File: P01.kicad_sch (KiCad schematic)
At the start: 63 parts

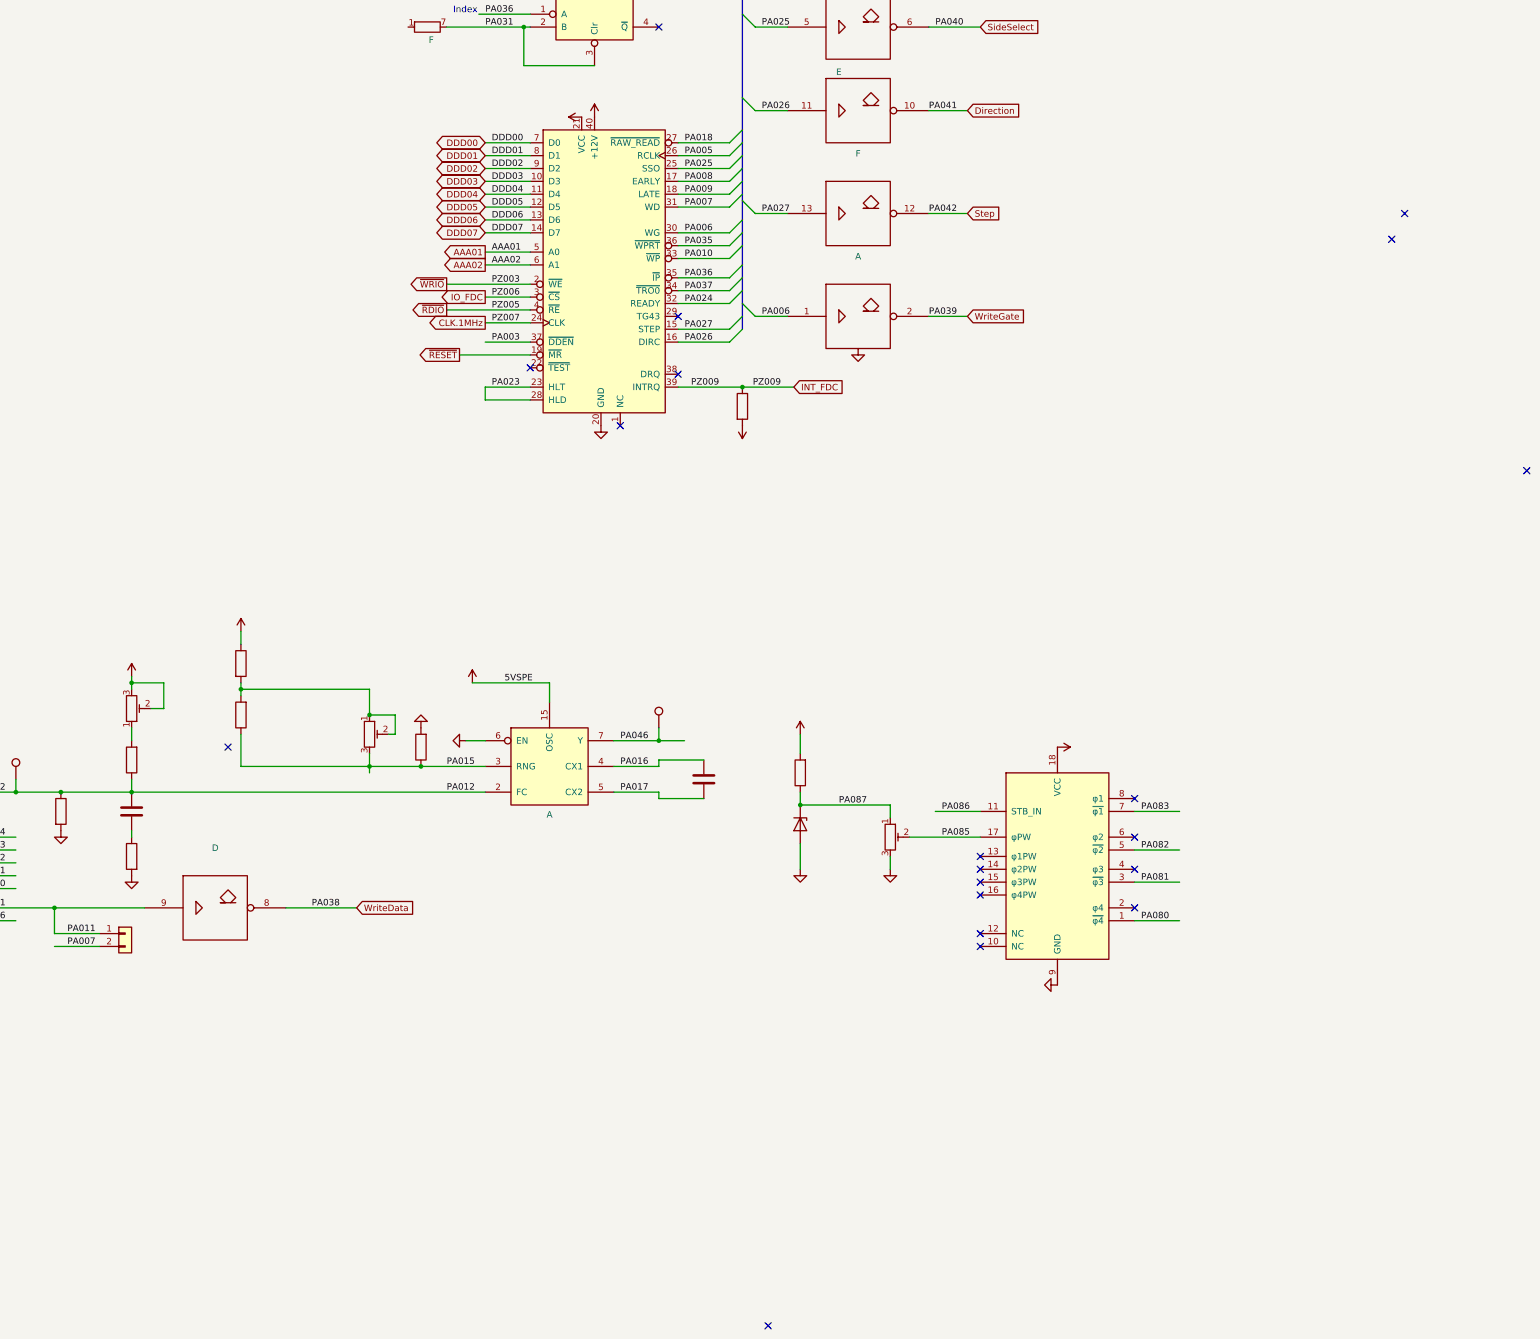
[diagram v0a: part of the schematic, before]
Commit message: fixing KiCad6 warnings
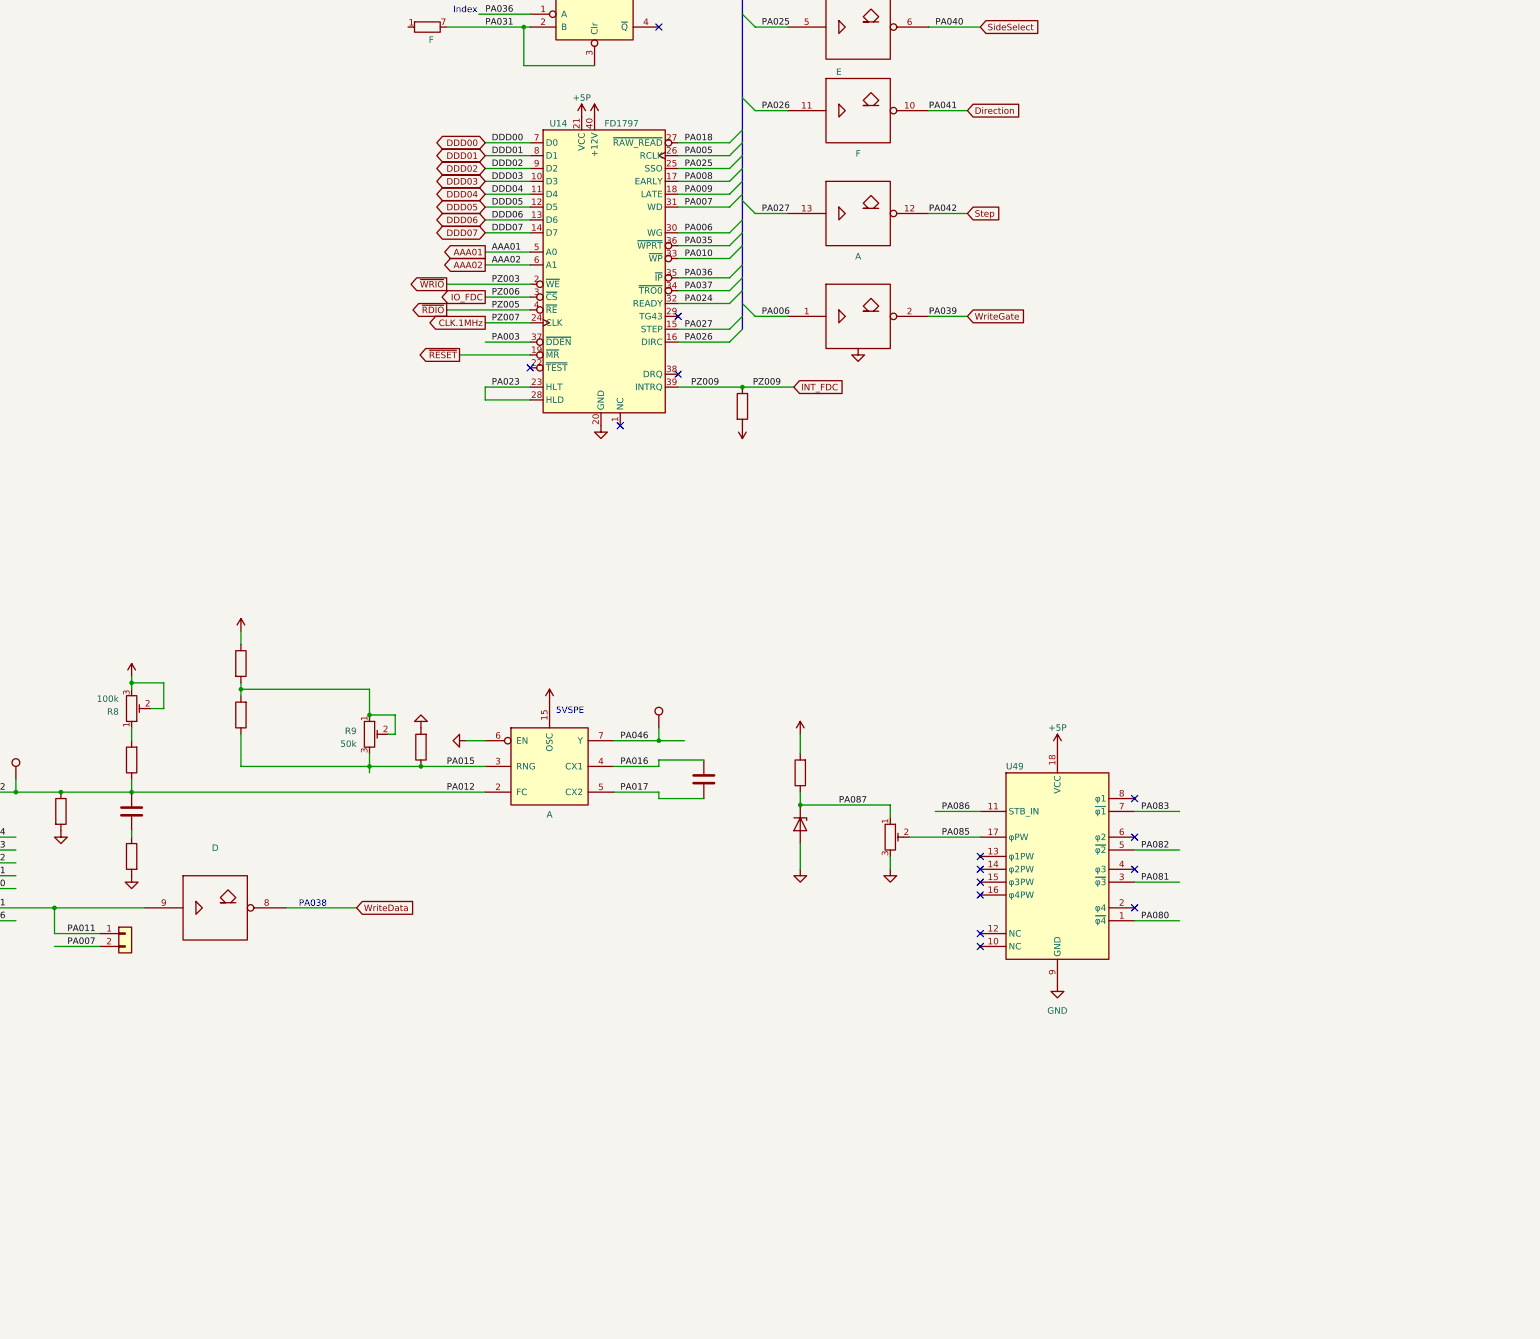
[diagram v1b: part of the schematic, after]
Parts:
- removed ?: (no value), symbol LOET.DE:FD1797
- removed ? (x2): (no value), symbol Device:R_POT_TRIM
- removed ?: (no value), symbol LOET.DE:WD2143M-03
- added R8: 100k, symbol Device:R_Potentiometer_Trim
- added R9: 50k, Potentiometer_THT:Potentiometer_Vishay_T73XW_Horizontal, symbol Device:R_Potentiometer_Trim
- added U14: FD1797, Package_DIP:DIP-40_W15.24mm, symbol M20:FD1797
- added U49: ~, symbol M20:WD2143M-03
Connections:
- net +12V: now also U14.40 (+12V)
- net +5P: now also U14.21 (VCC), U49.18 (VCC)
- net +5VA: now also R8.2, R8.3
- net AAA01: now also U14.5 (A0)
- net AAA02: now also U14.6 (A1)
- net CLK.1MHz: now also U14.24 (CLK)
- net DDD00: now also U14.7 (D0)
- net DDD01: now also U14.8 (D1)
- net DDD02: now also U14.9 (D2)
- net DDD03: now also U14.10 (D3)
- net DDD04: now also U14.11 (D4)
- net DDD05: now also U14.12 (D5)
- net DDD06: now also U14.13 (D6)
- net DDD07: now also U14.14 (D7)
- net GND: now also U14.20 (GND), U49.9 (GND)
- net INT_FDC: now also U14.39 (INTRQ)
- net IO_FDC: now also U14.3 (~{CS})
- net Index: now also U14.35 (~{IP})
- net PA003: now also U14.37 (~{DDEN})
- net PA005: now also U14.26 (RCLK)
- net PA006: now also U14.30 (WG)
- net PA007: now also U14.31 (WD)
- net PA008: now also U14.17 (EARLY)
- net PA009: now also U14.18 (LATE)
- net PA010: now also U14.33 (~{WP})
- net PA015: now also R9.3
- net PA018: now also U14.27 (~{RAW_READ})
- net PA023: now also U14.23 (HLT), U14.28 (HLD)
- net PA024: now also U14.32 (READY)
- net PA025: now also U14.25 (SSO)
- net PA026: now also U14.16 (DIRC)
- net PA027: now also U14.15 (STEP)
- net PA080: now also U49.1 (~{φ4})
- net PA081: now also U49.3 (~{φ3})
- net PA082: now also U49.5 (~{φ2})
- net PA083: now also U49.7 (~{φ1})
- net PA085: now also U49.17 (φPW)
- net PA086: now also U49.11 (STB_IN)
- net Track0: now also U14.34 (~{TRO0})
- net WriteProtect: now also U14.36 (~{WPRT})
- net ~{RDIO}: now also U14.4 (~{RE})
- net ~{RESET}: now also U14.19 (~{MR})
- net ~{WRIO}: now also U14.2 (~{WE})
- net at ?.2: now also R8.1
- net at ?.2, ?.2: now also R9.1, R9.2
- no-connect marks 36 -> 31
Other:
- note added: "5VSPE"
- note added: "PA038"
